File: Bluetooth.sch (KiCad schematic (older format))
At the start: 4 parts, among them P1 CONN_01X01, P5 CONN_01X06

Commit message: añaadido zocalo para sensor de temperatura y primera distribucion sobre la PCB
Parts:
- P1: footprint (none) -> Socket_Strips:Socket_Strip_Straight_1x01
- P5: footprint (none) -> Socket_Strips:Socket_Strip_Straight_1x06
- R29, R30: footprint (none) -> Resistors_SMD:R_0805

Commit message: finalizado enrutado provisional
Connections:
- net A2: no longer names the net of P5.1 (P1)
- no-connect marks 1 -> 2
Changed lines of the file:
@@
 $Descr User 8268 5846
 encoding utf-8
-Sheet 12 14
+Sheet 11 15
 Title ""
 Date ""
@@
 $EndComp
 Wire Wire Line
-	3150 2000 3650 2000
-Wire Wire Line
 	3150 2300 3650 2300
 Wire Wire Line
 	2800 2400 3650 2400
 Wire Wire Line
-	3150 2500 3650 2500
-Wire Wire Line
 	3650 2200 3500 2200
 Wire Wire Line
 	3500 2200 3500 3050
 $Comp
-L GND #PWR043
+L GND #PWR036
 U 1 1 5794D486
 P 3500 3050
-F 0 "#PWR043" H 3500 2800 50  0001 C CNN
+F 0 "#PWR036" H 3500 2800 50  0001 C CNN
 F 1 "GND" H 3505 2877 50  0000 C CNN
 F 2 "" H 3500 3050 50  0000 C CNN
@@
 	3500 2100 3500 1700
 $Comp
-L VCC #PWR044
+L VCC #PWR037
 U 1 1 5794D4A8
 P 3500 1700
-F 0 "#PWR044" H 3500 1550 50  0001 C CNN
+F 0 "#PWR037" H 3500 1550 50  0001 C CNN
 F 1 "VCC" H 3517 1873 50  0000 C CNN
 F 2 "" H 3500 1700 50  0000 C CNN
@@
 	2400 2900 2400 3050
 $Comp
-L GND #PWR045
+L GND #PWR038
 U 1 1 5794D54D
 P 2400 3050
-F 0 "#PWR045" H 2400 2800 50  0001 C CNN
+F 0 "#PWR038" H 2400 2800 50  0001 C CNN
 F 1 "GND" H 2405 2877 50  0000 C CNN
 F 2 "" H 2400 3050 50  0000 C CNN
@@
 Wire Wire Line
 	2200 2400 2500 2400
-NoConn ~ 3150 2500
+NoConn ~ 3650 2500
 Text GLabel 3150 2300 0    60   Input ~ 0
 D0
-Text GLabel 3150 2000 0    60   Input ~ 0
-A2
 Text GLabel 2200 2400 0    60   Input ~ 0
 D1
@@
 Text GLabel 3150 2650 0    60   Input ~ 0
 RESET
+NoConn ~ 3650 2000
 $EndSCHEMATC

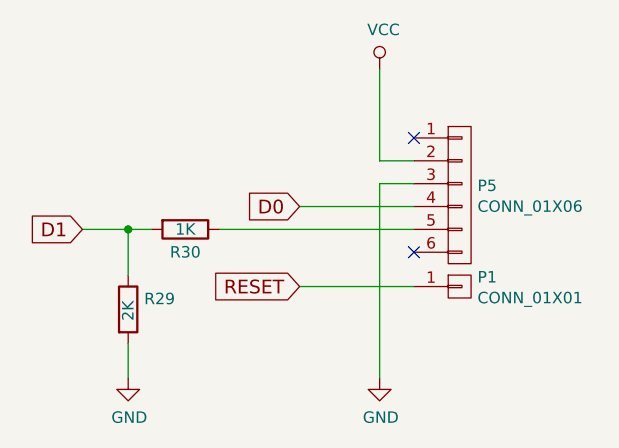
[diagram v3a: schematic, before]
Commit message: ordenar referencias de componentes
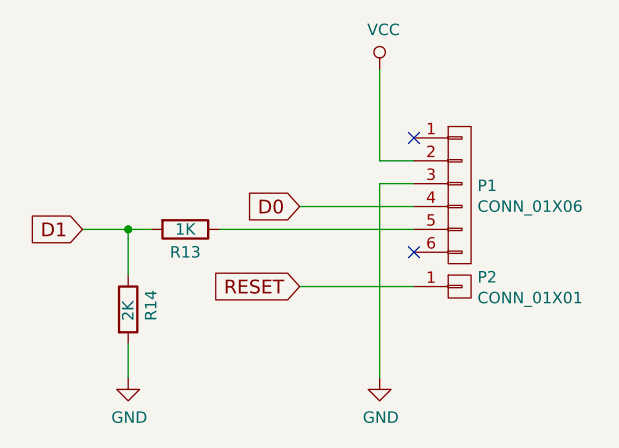
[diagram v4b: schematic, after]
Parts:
- P1: renamed from P5; Fabricante (none) -> NINIGI; Provedor (none) -> TME; Ref (none) -> ZL262-40SG; Ref_Proveedor (none) -> ZL262-40SG
- P2: renamed from P1; Fabricante (none) -> NINIGI; Provedor (none) -> TME; Ref (none) -> ZL262-40SG; Ref_Proveedor (none) -> ZL262-40SG
- R13: renamed from R30; Fabricante (none) -> VISHAY; Provedor (none) -> TME; Ref (none) -> CRCW08051K00FKEA; Ref_Proveedor (none) -> CRCW08051K00FKEA
- R14: renamed from R29; Fabricante (none) -> VISHAY; Provedor (none) -> TME; Ref (none) -> CRCW08052K00FKTABC; Ref_Proveedor (none) -> CRCW08052K00FKTABC
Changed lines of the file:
@@
 $Descr User 8268 5846
 encoding utf-8
-Sheet 11 15
+Sheet 5 15
 Title ""
 Date ""
@@
 $EndDescr
 $Comp
-L CONN_01X06 P5
+L CONN_01X06 P1
 U 1 1 5794D384
 P 3850 2250
-F 0 "P5" H 3928 2291 50  0000 L CNN
+F 0 "P1" H 3928 2291 50  0000 L CNN
 F 1 "CONN_01X06" H 3928 2200 50  0000 L CNN
 F 2 "Socket_Strips:Socket_Strip_Straight_1x06" H 3850 2250 50  0001 C CNN
 F 3 "" H 3850 2250 50  0000 C CNN
-F 4 "~" H 3850 2250 60  0001 C CNN "Fabricante"
-F 5 "~" H 3850 2250 60  0001 C CNN "Ref"
+F 4 "NINIGI" H 3850 2250 60  0001 C CNN "Fabricante"
+F 5 "ZL262-40SG" H 3850 2250 60  0001 C CNN "Ref"
 F 6 "~" H 3850 2250 60  0001 C CNN "Potencia"
 F 7 "~" H 3850 2250 60  0001 C CNN "Tolerancia"
-F 8 "~" H 3850 2250 60  0001 C CNN "Provedor"
-F 9 "~" H 3850 2250 60  0001 C CNN "Ref_Proveedor"
+F 8 "TME" H 3850 2250 60  0001 C CNN "Provedor"
+F 9 "ZL262-40SG" H 3850 2250 60  0001 C CNN "Ref_Proveedor"
 	1    3850 2250
 	1    0    0    -1
@@
 	3500 2200 3500 3050
 $Comp
-L GND #PWR036
+L GND #PWR17
 U 1 1 5794D486
 P 3500 3050
-F 0 "#PWR036" H 3500 2800 50  0001 C CNN
+F 0 "#PWR17" H 3500 2800 50  0001 C CNN
 F 1 "GND" H 3505 2877 50  0000 C CNN
 F 2 "" H 3500 3050 50  0000 C CNN
@@
 	3500 2100 3500 1700
 $Comp
-L VCC #PWR037
+L VCC #PWR16
 U 1 1 5794D4A8
 P 3500 1700
-F 0 "#PWR037" H 3500 1550 50  0001 C CNN
+F 0 "#PWR16" H 3500 1550 50  0001 C CNN
 F 1 "VCC" H 3517 1873 50  0000 C CNN
 F 2 "" H 3500 1700 50  0000 C CNN
@@
 $EndComp
 $Comp
-L R R30
+L R R13
 U 1 1 5794D4BE
 P 2650 2400
-F 0 "R30" V 2750 2400 50  0000 C CNN
+F 0 "R13" V 2750 2400 50  0000 C CNN
 F 1 "1K" V 2650 2400 50  0000 C CNN
 F 2 "Resistors_SMD:R_0805" V 2580 2400 50  0001 C CNN
 F 3 "" H 2650 2400 50  0000 C CNN
+F 4 "VISHAY" H 2650 2400 60  0001 C CNN "Fabricante"
+F 5 "CRCW08051K00FKEA" H 2650 2400 60  0001 C CNN "Ref"
+F 6 "~" H 2650 2400 60  0001 C CNN "Potencia"
+F 7 "~" H 2650 2400 60  0001 C CNN "Tolerancia"
+F 8 "TME" H 2650 2400 60  0001 C CNN "Provedor"
+F 9 "CRCW08051K00FKEA" H 2650 2400 60  0001 C CNN "Ref_Proveedor"
 	1    2650 2400
 	0    1    1    0
 $EndComp
 $Comp
-L R R29
+L R R14
 U 1 1 5794D4FD
 P 2400 2750
-F 0 "R29" H 2470 2796 50  0000 L CNN
+F 0 "R14" V 2500 2700 50  0000 L CNN
 F 1 "2K" V 2400 2700 50  0000 L CNN
 F 2 "Resistors_SMD:R_0805" V 2330 2750 50  0001 C CNN
 F 3 "" H 2400 2750 50  0000 C CNN
+F 4 "VISHAY" H 2400 2750 60  0001 C CNN "Fabricante"
+F 5 "CRCW08052K00FKTABC" H 2400 2750 60  0001 C CNN "Ref"
+F 6 "~" H 2400 2750 60  0001 C CNN "Potencia"
+F 7 "~" H 2400 2750 60  0001 C CNN "Tolerancia"
+F 8 "TME" H 2400 2750 60  0001 C CNN "Provedor"
+F 9 "CRCW08052K00FKTABC" H 2400 2750 60  0001 C CNN "Ref_Proveedor"
 	1    2400 2750
 	1    0    0    -1
@@
 	2400 2900 2400 3050
 $Comp
-L GND #PWR038
+L GND #PWR15
 U 1 1 5794D54D
 P 2400 3050
-F 0 "#PWR038" H 2400 2800 50  0001 C CNN
+F 0 "#PWR15" H 2400 2800 50  0001 C CNN
 F 1 "GND" H 2405 2877 50  0000 C CNN
 F 2 "" H 2400 3050 50  0000 C CNN
@@
 00 EC 06 C4 28 00 00 00 00 00 D8 0D 88 51 00 00 00 00 00 B0 1B 10 A3 00 00 00 00 00 60 37 20 46
 01 00 00 00 00 C0 6E 40 8C 02 00 00 00 00 80 DD F8 FF 78 25 BB 0D 57 C7 E7 CD 00 00 00 00 49 45
-4E 44 AE 42 60 82 00
+4E 44 AE 42 60 82 55
 EndData
 $EndBitmap
 $Comp
-L CONN_01X01 P1
+L CONN_01X01 P2
 U 1 1 5795457D
 P 3850 2650
-F 0 "P1" H 3928 2691 50  0000 L CNN
+F 0 "P2" H 3928 2691 50  0000 L CNN
 F 1 "CONN_01X01" H 3928 2600 50  0000 L CNN
 F 2 "Socket_Strips:Socket_Strip_Straight_1x01" H 3850 2650 50  0001 C CNN
 F 3 "" H 3850 2650 50  0000 C CNN
+F 4 "NINIGI" H 3850 2650 60  0001 C CNN "Fabricante"
+F 5 "ZL262-40SG" H 3850 2650 60  0001 C CNN "Ref"
+F 6 "~" H 3850 2650 60  0001 C CNN "Potencia"
+F 7 "~" H 3850 2650 60  0001 C CNN "Tolerancia"
+F 8 "TME" H 3850 2650 60  0001 C CNN "Provedor"
+F 9 "ZL262-40SG" H 3850 2650 60  0001 C CNN "Ref_Proveedor"
 	1    3850 2650
 	1    0    0    -1

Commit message: cambiados encoder y potenciometro
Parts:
- R13, R14: footprint Resistors_SMD:R_0805 -> Resistencias:R_0805
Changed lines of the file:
@@
 	3500 2200 3500 3050
 $Comp
-L GND #PWR17
+L GND #PWR017
 U 1 1 5794D486
 P 3500 3050
-F 0 "#PWR17" H 3500 2800 50  0001 C CNN
+F 0 "#PWR017" H 3500 2800 50  0001 C CNN
 F 1 "GND" H 3505 2877 50  0000 C CNN
 F 2 "" H 3500 3050 50  0000 C CNN
@@
 	3500 2100 3500 1700
 $Comp
-L VCC #PWR16
+L VCC #PWR018
 U 1 1 5794D4A8
 P 3500 1700
-F 0 "#PWR16" H 3500 1550 50  0001 C CNN
+F 0 "#PWR018" H 3500 1550 50  0001 C CNN
 F 1 "VCC" H 3517 1873 50  0000 C CNN
 F 2 "" H 3500 1700 50  0000 C CNN
@@
 F 0 "R13" V 2750 2400 50  0000 C CNN
 F 1 "1K" V 2650 2400 50  0000 C CNN
-F 2 "Resistors_SMD:R_0805" V 2580 2400 50  0001 C CNN
+F 2 "Resistencias:R_0805" V 2580 2400 50  0001 C CNN
 F 3 "" H 2650 2400 50  0000 C CNN
 F 4 "VISHAY" H 2650 2400 60  0001 C CNN "Fabricante"
@@
 F 0 "R14" V 2500 2700 50  0000 L CNN
 F 1 "2K" V 2400 2700 50  0000 L CNN
-F 2 "Resistors_SMD:R_0805" V 2330 2750 50  0001 C CNN
+F 2 "Resistencias:R_0805" V 2330 2750 50  0001 C CNN
 F 3 "" H 2400 2750 50  0000 C CNN
 F 4 "VISHAY" H 2400 2750 60  0001 C CNN "Fabricante"
@@
 	2400 2900 2400 3050
 $Comp
-L GND #PWR15
+L GND #PWR019
 U 1 1 5794D54D
 P 2400 3050
-F 0 "#PWR15" H 2400 2800 50  0001 C CNN
+F 0 "#PWR019" H 2400 2800 50  0001 C CNN
 F 1 "GND" H 2405 2877 50  0000 C CNN
 F 2 "" H 2400 3050 50  0000 C CNN

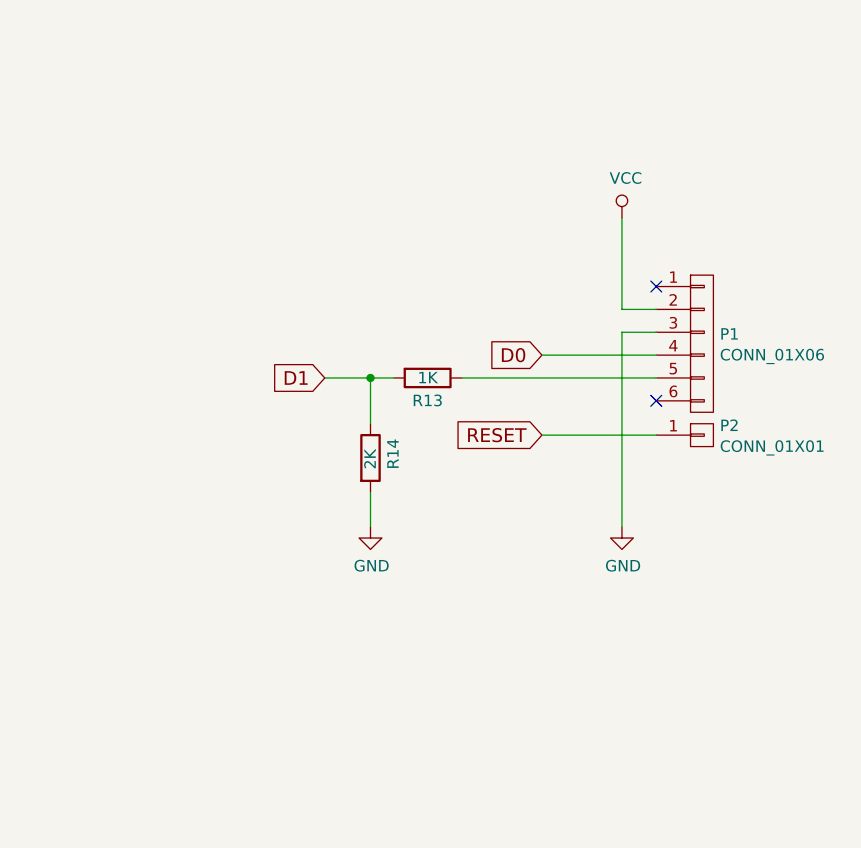
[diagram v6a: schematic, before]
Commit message: añadidos driver para led y conectores para fotodiodos infrarrojos
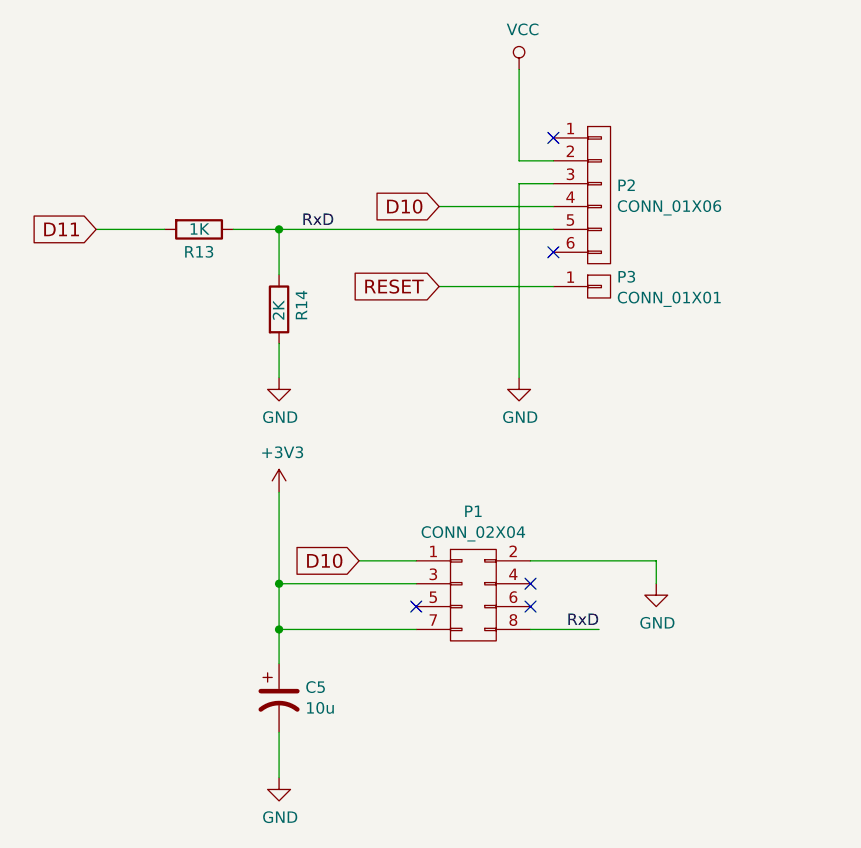
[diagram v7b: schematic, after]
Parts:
- added C5: 10u, Capacitors_Tantalum_SMD:Tantalum_Case-A_EIA-3216-18_Reflow, symbol CP1
- added P1: CONN_02X04, Socket_Strips:Socket_Strip_Straight_2x04, symbol CONN_02X04
- P2: renamed from P1; Ref ZL262-40SG -> ZL262-6SG; Ref_Proveedor ZL262-40SG -> ZL262-6SG
- renumbered P2 to P3
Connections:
- net GND: now also C5.2, P1.2 (P2)
- net RxD: now reaches P2.5 (P5), R13.1
- net RxD: now also R14.1, P1.8 (P8)
- net D0 renamed D10
- net D10: now also P1.1 (P1)
- net D1 renamed D11
- net D11: no longer R14.1
- new net +3V3: C5.1, P1.3 (P3), P1.7 (P7)
- no-connect marks 2 -> 5
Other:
- moved on the sheet: P2, P3, R13, R14

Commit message: modificada posicion del modulo esp
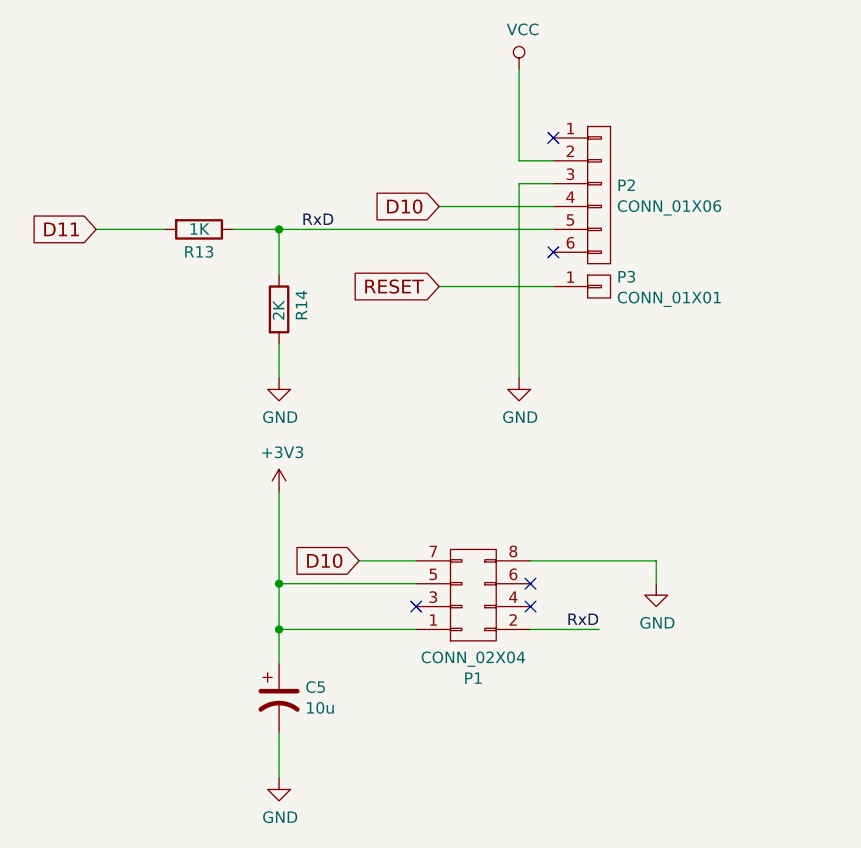
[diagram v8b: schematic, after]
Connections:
- net +3V3: now also P1.1 (P1), P1.5 (P5); no longer P1.3 (P3), P1.7 (P7)
- net D10: now also P1.7 (P7); no longer P1.1 (P1)
- net GND: now also P1.8 (P8); no longer P1.2 (P2)
- net RxD: now also P1.2 (P2); no longer P1.8 (P8)
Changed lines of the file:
@@
 F 9 "ZL262-8DG" H 2850 3350 60  0001 C CNN "Ref_Proveedor"
 	1    2850 3350
-	1    0    0    -1
+	1    0    0    1
 $EndComp
 $Comp
